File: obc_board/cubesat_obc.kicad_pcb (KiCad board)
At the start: 4 copper layers, 92 x 88.9 mm, 243 parts, among them J10 FSI-110-03-X-D-AD-SD-K-TR, J17 Micro_SD_Card, J9 FSI-110-03-X-D-AD-SD-K-TR, U1 ADG1607, U10 MMC5983MA, U11 LTC4304CMSTRPBF, U12 LTC4304CMSTRPBF, U13 LTC4304CMSTRPBF, U14 PC104, U15 LTC4304CMSTRPBF, U16 MAX14830, U17 AP2127N-3.3, U18 FT4232H-56Q-REEL, U19 STM32L552ZET6Q, U2 AT45DB041E-SSHN-B, U20 MMC5983MA, U21 NCV7723DQBR2G, U3 AT45DB041E-SSHN-B, U4 LTC4304CMSTRPBF, U5 MCP9600-E_MX, U6 LT3483ES6, U7 BMI090L, U8 BMI090L, U9 MMC5983MA, Y1 4MHz, Y2 12MHz, Y3 8MHz, Y4 32.768kHz

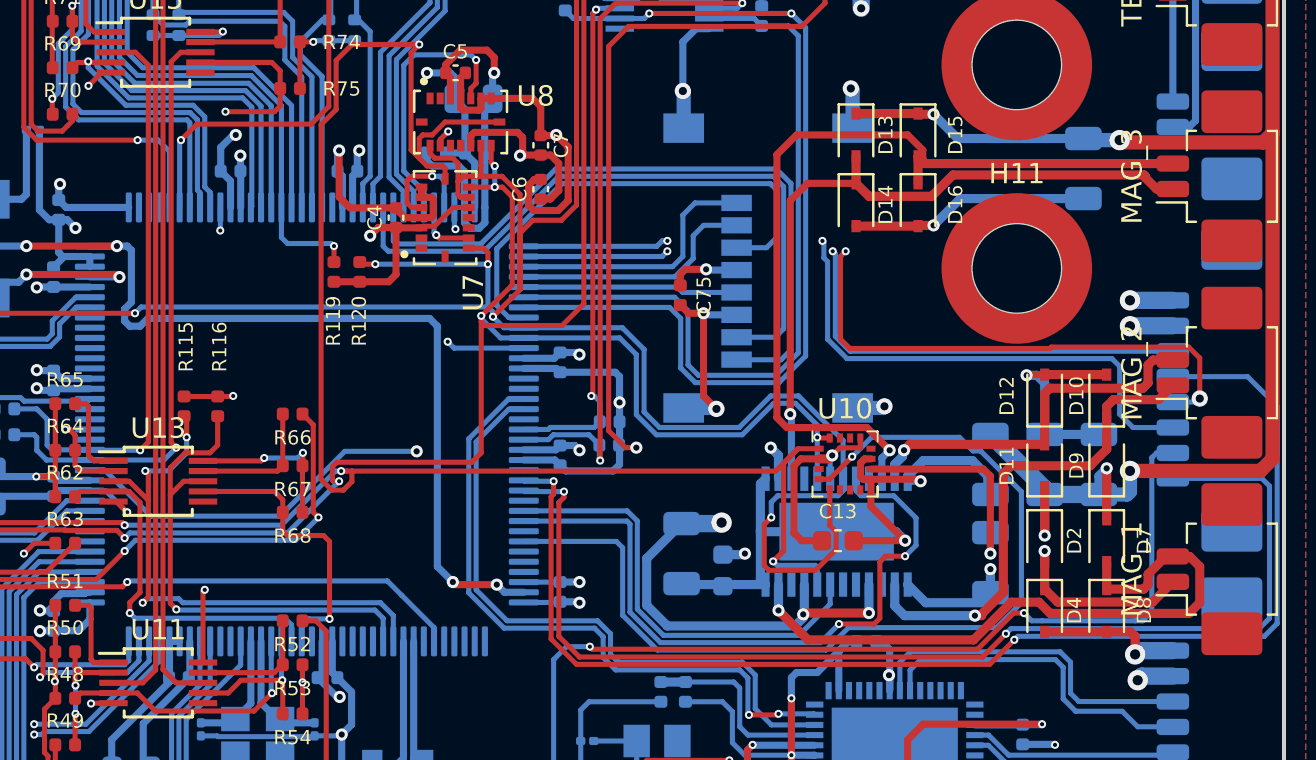
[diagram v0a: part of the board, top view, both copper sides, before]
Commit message: reduce via
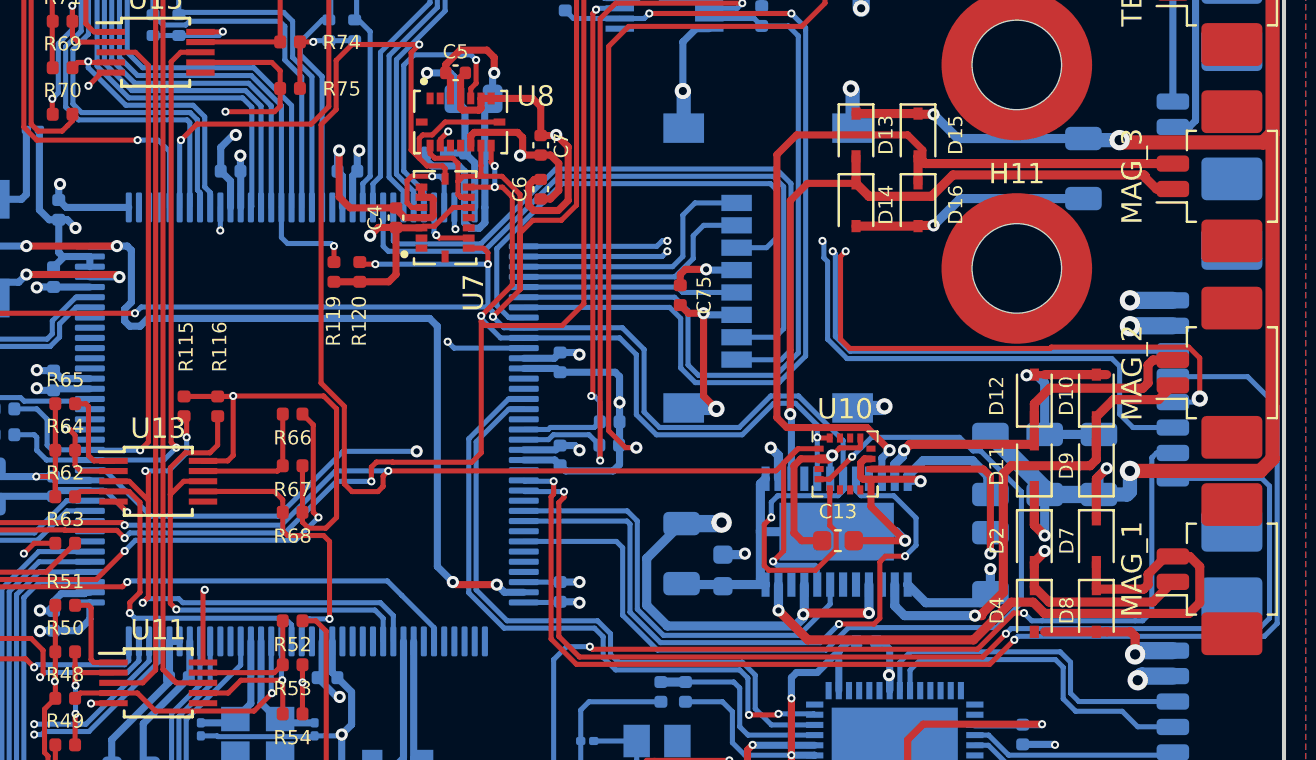
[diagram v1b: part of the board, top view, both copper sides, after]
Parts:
- moved D10 0.51 mm to (190.4, 104.5)
- moved D11 0.51 mm to (187.3, 108.0)
- moved D12 0.51 mm to (187.3, 104.5)
- moved D2 0.51 mm to (187.3, 111.6)
- moved D4 0.51 mm to (187.3, 115.1)
- moved D7 0.51 mm to (190.4, 111.6)
- moved D8 0.51 mm to (190.4, 115.1)
- moved D9 0.51 mm to (190.4, 108.0)
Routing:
- net /3V3_3: track 289.0 -> 301.0 mm, vias 41 -> 39
- net /SCK_2: track 227.9 -> 229.2 mm
- net Net-(D2-Pad2): track 28.2 -> 28.9 mm
- net /MOSI_2: track 211.9 -> 211.3 mm
- net Net-(D7-Pad2): track 32.6 -> 33.1 mm

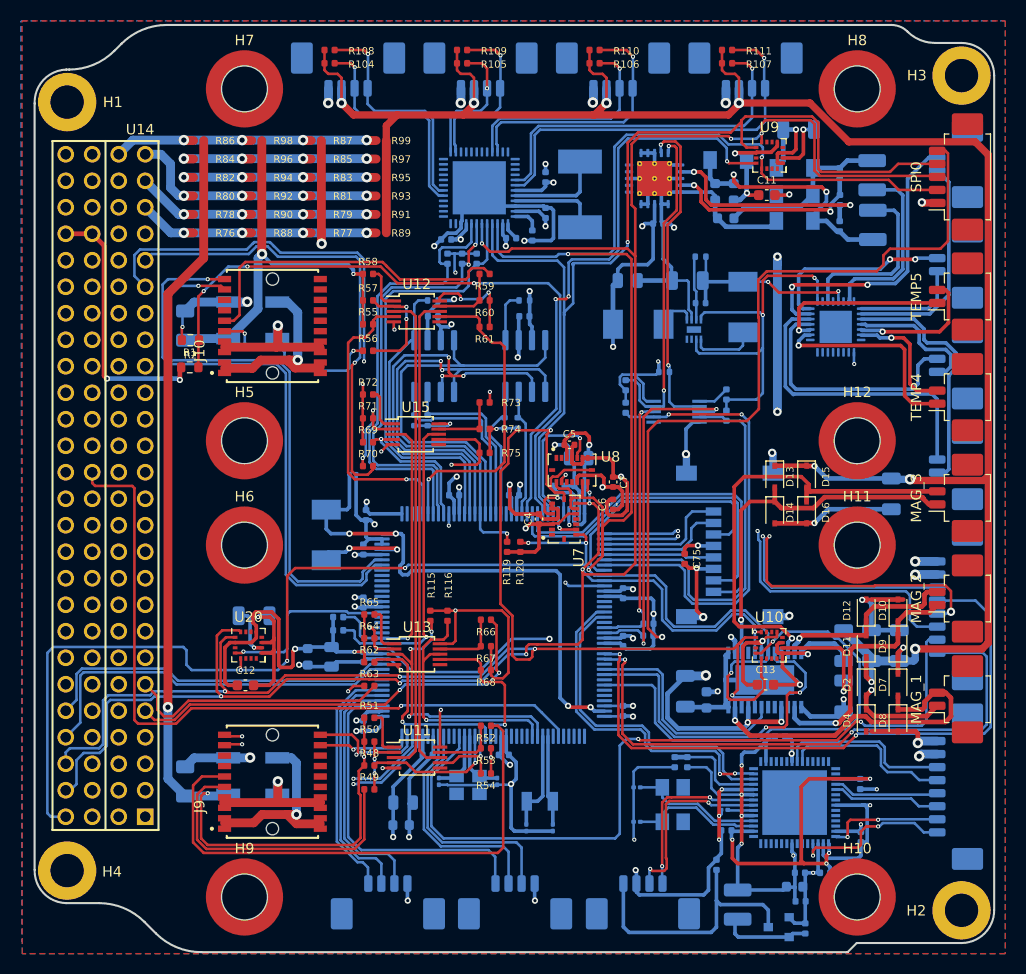
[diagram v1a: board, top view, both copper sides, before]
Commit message: reduce via
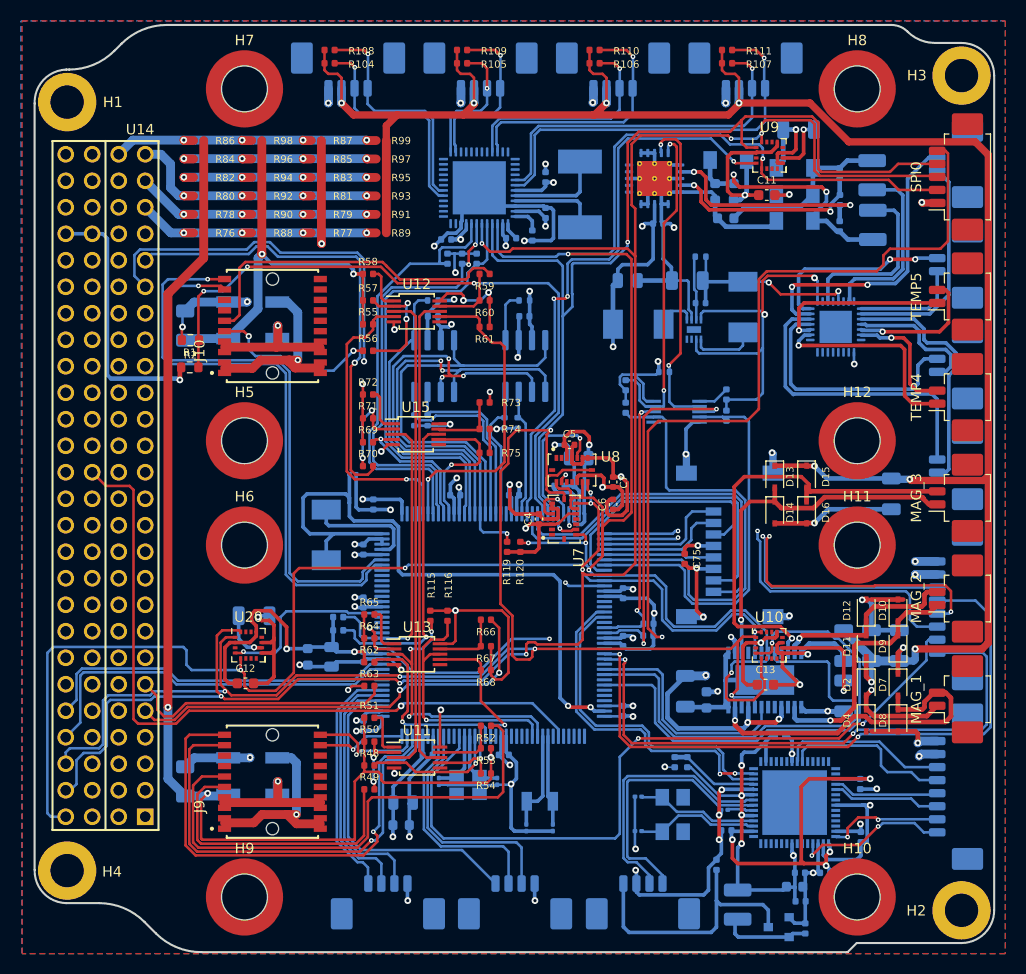
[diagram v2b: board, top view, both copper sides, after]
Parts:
- moved C68 1.23 mm to (140.1, 94.4)
- moved Y2 0.95 mm to (168.8, 124.1)
- moved C41 0.90 mm to (165.5, 122.4)
- moved C40 0.90 mm to (165.5, 125.7)
- moved C12 0.19 mm to (127.8, 111.5)
- moved C57 0.10 mm to (147.9, 93.5)
- turned L10 to 270 degrees
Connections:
- U19 pad 114: /TEMP_ACC -> /TEMP_FAULT
- U19 pad 115: /TEMP_FAULT -> /TEMP_ACC
- USB0 pad 1: /ftdi/D+ -> /ftdi/D-
- USB0 pad 2: /ftdi/D- -> /ftdi/D+
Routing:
- net /RX1_OBC: track 23.3 -> 46.2 mm, vias 2 -> 1
- net GND: track 415.3 -> 393.4 mm
- net /TX1_OBC: track 23.9 -> 43.8 mm, vias 2 -> 1
- net Net-(C74-Pad2): track 52.3 -> 64.0 mm, vias 4 -> 2
- net /MAGT_EN: track 33.3 -> 43.1 mm, vias 2 -> 0
- net /ftdi/D+: track 16.9 -> 25.1 mm, vias 2 -> 0
- net /ftdi/D-: track 18.1 -> 25.3 mm, vias 2 -> 0
- net /mcu/NRST: track 76.4 -> 71.9 mm
- net /MISO_2: track 242.6 -> 245.9 mm, vias 9 -> 8
- net /3V3_3: track 301.0 -> 303.9 mm, vias 39 -> 38
- net Net-(L10-Pad1): track 9.13 -> 10.9 mm, vias 2 -> 0
- net /TEMP_FAULT: track 45.8 -> 44.2 mm, vias 2 -> 0
- net /ADC3: track 32.8 -> 31.2 mm
- net /FAULT4: track 15.7 -> 14.2 mm, vias 2 -> 1
- net Net-(J9-Pad11): track 51.7 -> 50.2 mm
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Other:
- net class power added: clearance 0.11, trace_width 0.35, via_dia 0.65, via_drill 0.3
- net class signal added: clearance 0.11, trace_width 0.35, via_dia 0.45, via_drill 0.2
- rule via_min_size: 0.4 -> 0.45

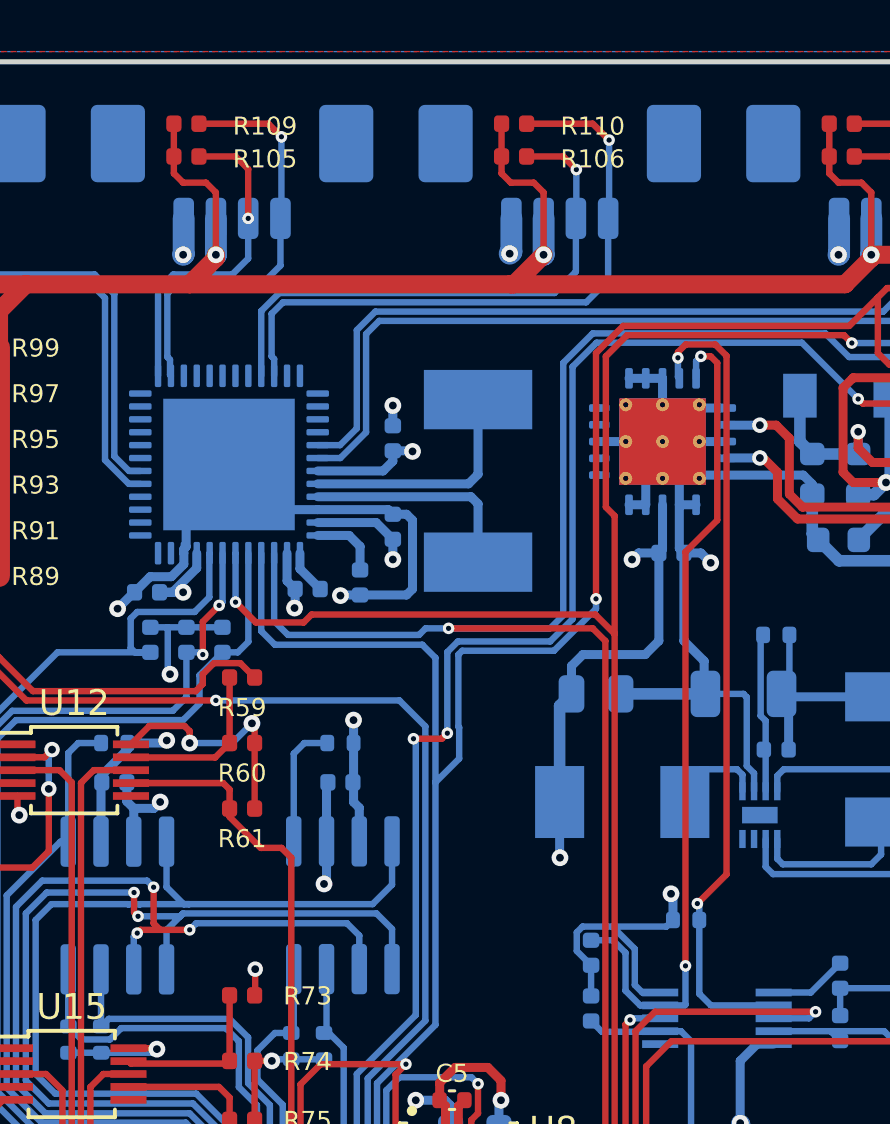
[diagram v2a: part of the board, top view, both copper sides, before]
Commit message: major obc schematic revision, added adapter board
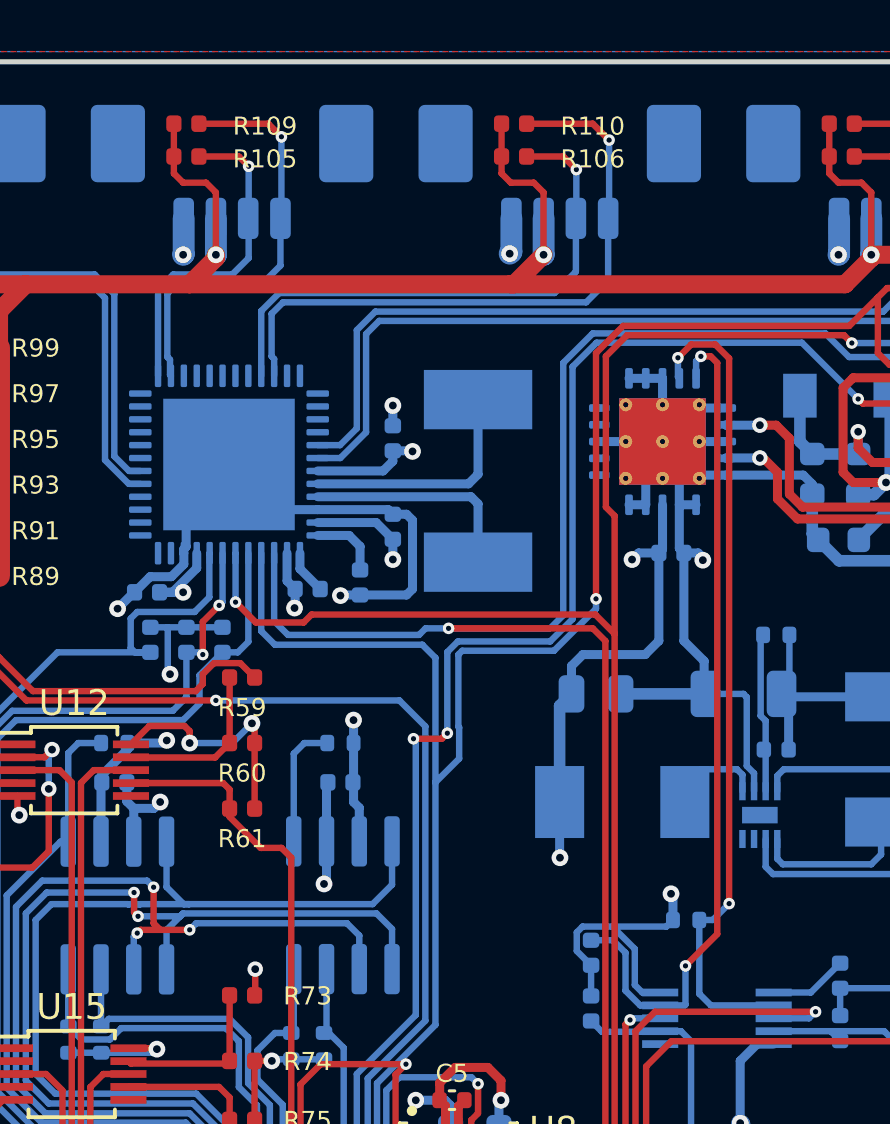
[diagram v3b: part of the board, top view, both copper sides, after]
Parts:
- added G***: LOGO, cubesat_obc:nush, B.Cu at (133.5, 88.3)
- added Ref**: Val**, cubesat_obc:logo, F.Cu at (131.2, 64.0)
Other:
- board text added: "OBC Board V1.0"
- board text added: "by Lin Yicheng"
